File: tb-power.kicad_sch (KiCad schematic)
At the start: 56 parts, among them Q1 BC817-25W, U4 JHL6340SLLSQ

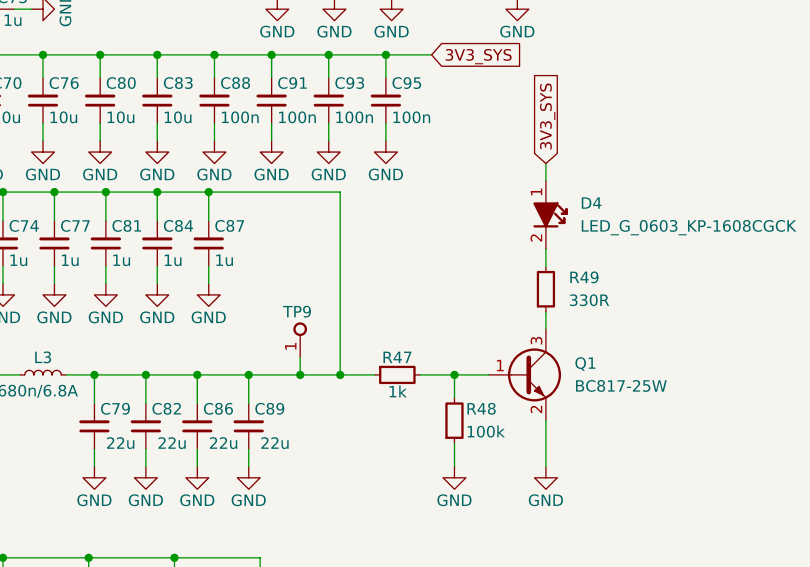
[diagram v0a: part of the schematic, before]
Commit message: Added switches for toggling PCIe power
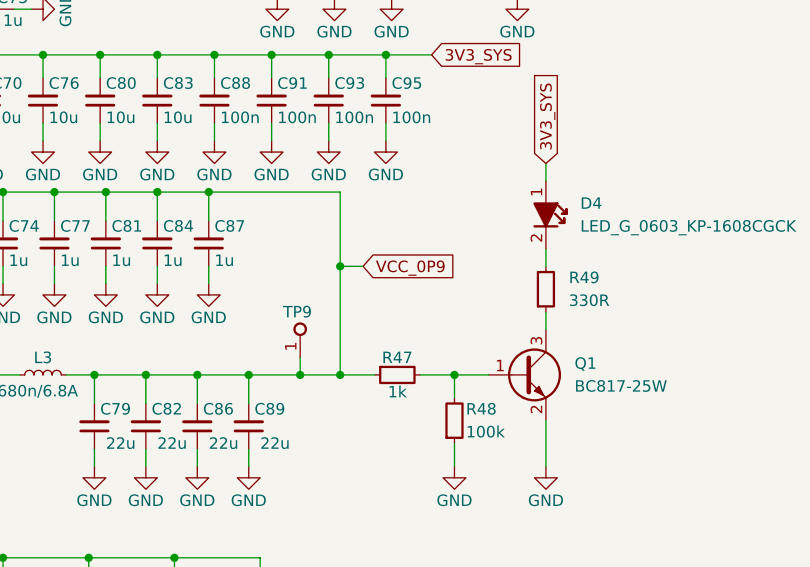
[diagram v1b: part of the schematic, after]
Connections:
- net VCC_0P9: now reaches C74.2, C77.2, C79.2, C81.2, C82.2, C84.2, C86.2, C87.2, C89.2, L3.2, R47.1, TP9.1, U4.E12 (VCC0P9_SVR_ANA), U4.E13 (VCC0P9_SVR_ANA), U4.F11 (VCC0P9_SVR_ANA), U4.F12 (VCC0P9_SVR_ANA), U4.F13 (VCC0P9_SVR_ANA), U4.F15 (VCC0P9_SVR_ANA), U4.J9 (VCC0P9_SVR_SENSE), U4.L9 (VCC0P9_SVR), U4.M9 (VCC0P9_SVR)
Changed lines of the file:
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@@
   (junction (at 174.625 85.09) (diameter 0) (color 0 0 0 0)
   )
+  (junction (at 218.44 113.665) (diameter 0) (color 0 0 0 0)
+  )
   (junction (at 116.205 92.71) (diameter 0) (color 0 0 0 0)
   )
@@
     (stroke (width 0) (type default) (color 0 0 0 0))
   )
+  (wire (pts (xy 218.44 113.665) (xy 218.44 125.73))
+    (stroke (width 0) (type default) (color 0 0 0 0))
+  )
   (wire (pts (xy 187.96 71.12) (xy 174.625 71.12))
     (stroke (width 0) (type default) (color 0 0 0 0))
@@
     (stroke (width 0) (type default) (color 0 0 0 0))
   )
-  (wire (pts (xy 218.44 105.41) (xy 218.44 125.73))
+  (wire (pts (xy 218.44 105.41) (xy 218.44 113.665))
     (stroke (width 0) (type default) (color 0 0 0 0))
   )
@@
   )
   (wire (pts (xy 175.26 265.43) (xy 175.26 267.97))
+    (stroke (width 0) (type default) (color 0 0 0 0))
+  )
+  (wire (pts (xy 218.44 113.665) (xy 220.98 113.665))
     (stroke (width 0) (type default) (color 0 0 0 0))
   )
@@
     (effects (font (size 2.54 2.54) (thickness 0.508) bold) (justify left bottom))
   )
+  (global_label "VCC_0P9" (shape input) (at 220.98 113.665 0) (fields_autoplaced)
+    (effects (font (size 1.27 1.27)) (justify left))
+    (property "Intersheet References" "${INTERSHEET_REFS}" (id 0) (at 231.6783 113.5856 0)
+      (effects (font (size 1.27 1.27)) (justify left) hide)
+    )
+  )
   (global_label "3V3_SYS" (shape input) (at 187.96 71.12 0) (fields_autoplaced)

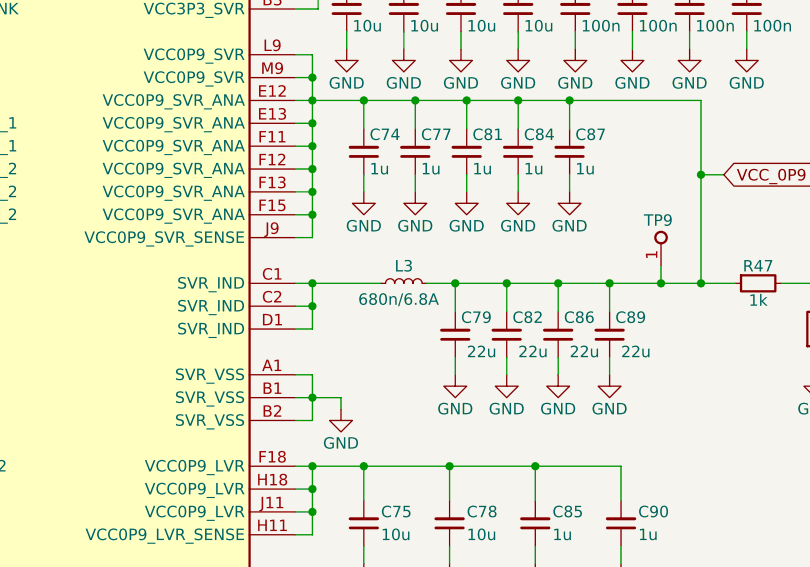
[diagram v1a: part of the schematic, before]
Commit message: [#49762] Fix missing 3D models
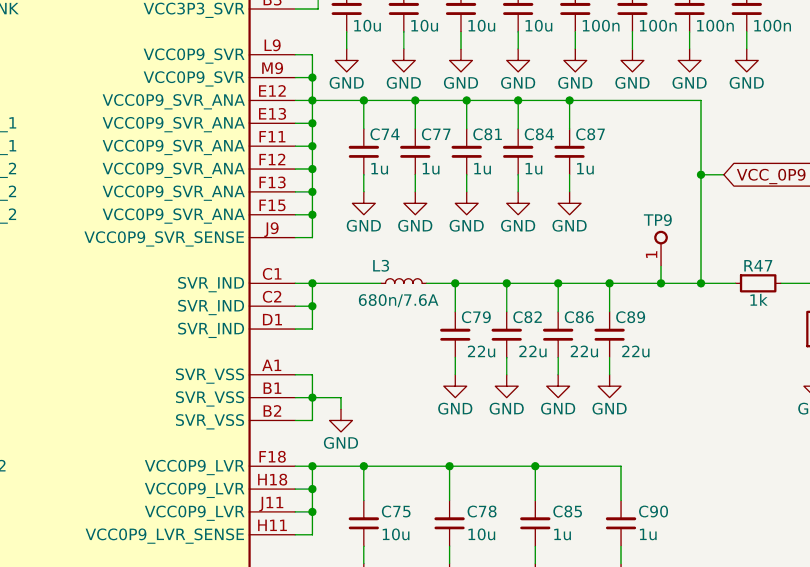
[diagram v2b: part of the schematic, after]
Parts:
- removed L3: L_680n_6.8A_IHLP1616BZ, antmicro-footprints:L_Vishay_IHLP1616BZ, symbol antmicroFixedInductors:L_680n_6.8A_IHLP1616BZ
- added L3: L_680n_7.6A_IHLP1616BZ, antmicro-footprints:L_Vishay-IHLP1616BZ, symbol antmicroFixedInductors:L_680n_7.6A_IHLP1616BZ
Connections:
- net VCC_0P9: now also L3.2
- net at U4.C1 (SVR_IND), U4.C2 (SVR_IND), U4.D1 (SVR_IND): now also L3.1
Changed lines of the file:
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@@
+    (pin "2")
+  )
+  (symbol (lib_id "antmicroFixedInductors:L_680n_7.6A_IHLP1616BZ") (at 182.88 125.73 0) (unit 1)
+    (in_bom yes) (on_board yes)
+    (property "Reference" "L3" (id 0) (at 182.88 123.825 0)
+      (effects (font (size 1.27 1.27) (thickness 0.15)))
+    )
+    (property "Value" "L_680n_7.6A_IHLP1616BZ" (id 1) (at 196.85 128.27 0)
+      (effects (font (size 1.27 1.27) (thickness 0.15)) (justify left bottom) hide)
+    )
+    (property "Footprint" "antmicro-footprints:L_Vishay-IHLP1616BZ" (id 2) (at 196.85 133.35 0)
+      (effects (font (size 1.27 1.27) (thickness 0.15)) (justify left bottom) hide)
+    )
+    (property "Datasheet" "https://www.mouser.com/datasheet/2/427/ihlp1616bz5a-1763007.pdf" (id 3) (at 196.85 135.89 0)
+      (effects (font (size 1.27 1.27) (thickness 0.15)) (justify left bottom) hide)
+    )
+    (property "Val" "680n/7.6A" (id 4) (at 184.785 127.635 0)
+      (effects (font (size 1.27 1.27) (thickness 0.15)))
+    )
+    (property "Manufacturer" "Vishay" (id 5) (at 196.85 138.43 0)
+      (effects (font (size 1.27 1.27) (thickness 0.15)) (justify left bottom) hide)
+    )
+    (property "MPN" "IHLP1616BZERR68M5A" (id 6) (at 196.85 140.97 0)
+      (effects (font (size 1.27 1.27) (thickness 0.15)) (justify left bottom) hide)
+    )
+    (property "ISat" "6.8 A" (id 7) (at 196.85 142.24 0)
+      (effects (font (size 1.27 1.27)) (justify left) hide)
+    )
+    (property "IMax" "7.6 A" (id 8) (at 196.85 146.05 0)
+      (effects (font (size 1.27 1.27) (thickness 0.15)) (justify left bottom) hide)
+    )
+    (property "Size" "4.06x4.06" (id 9) (at 196.85 148.59 0)
+      (effects (font (size 1.27 1.27) (thickness 0.15)) (justify left bottom) hide)
+    )
+    (property "Author" "Antmicro" (id 10) (at 196.85 151.13 0)
+      (effects (font (size 1.27 1.27) (thickness 0.15)) (justify left bottom) hide)
+    )
+    (property "License" "Apache-2.0" (id 11) (at 196.85 153.67 0)
+      (effects (font (size 1.27 1.27) (thickness 0.15)) (justify left bottom) hide)
+    )
+    (pin "1")
     (pin "2")
   )
@@
     (pin "1")
   )
-  (symbol (lib_id "antmicroFixedInductors:L_680n_6.8A_IHLP1616BZ") (at 182.88 125.73 0) (unit 1)
-    (in_bom yes) (on_board yes)
-    (property "Reference" "L3" (id 0) (at 185.42 123.825 0)
-      (effects (font (size 1.27 1.27) (thickness 0.15)))
-    )
-    (property "Value" "L_680n_6.8A_IHLP1616BZ" (id 1) (at 196.85 128.27 0)
-      (effects (font (size 1.27 1.27) (thickness 0.15)) (justify left bottom) hide)
-    )
-    (property "Footprint" "antmicro-footprints:L_Vishay_IHLP1616BZ" (id 2) (at 196.85 133.35 0)
-      (effects (font (size 1.27 1.27) (thickness 0.15)) (justify left bottom) hide)
-    )
-    (property "Datasheet" "https://www.mouser.pl/datasheet/2/427/ihlp1616bz5a-1763007.pdf" (id 3) (at 196.85 135.89 0)
-      (effects (font (size 1.27 1.27) (thickness 0.15)) (justify left bottom) hide)
-    )
-    (property "Val" "680n/6.8A" (id 4) (at 180.34 128.27 0)
-      (effects (font (size 1.27 1.27) (thickness 0.15)) (justify left bottom))
-    )
-    (property "Manufacturer" "Vishay" (id 5) (at 196.85 138.43 0)
-      (effects (font (size 1.27 1.27) (thickness 0.15)) (justify left bottom) hide)
-    )
-    (property "MPN" "IHLP1616BZERR68M5A" (id 6) (at 196.85 140.97 0)
-      (effects (font (size 1.27 1.27) (thickness 0.15)) (justify left bottom) hide)
-    )
-    (property "ISat" "6.8" (id 7) (at 196.85 142.24 0)
-      (effects (font (size 1.27 1.27)) (justify left) hide)
-    )
-    (property "IMax" "7.6" (id 8) (at 196.85 146.05 0)
-      (effects (font (size 1.27 1.27) (thickness 0.15)) (justify left bottom) hide)
-    )
-    (property "Size" "4.06x4.06" (id 9) (at 196.85 148.59 0)
-      (effects (font (size 1.27 1.27) (thickness 0.15)) (justify left bottom) hide)
-    )
-    (property "License" "Apache-2.0" (id 11) (at 196.85 153.67 0)
-      (effects (font (size 1.27 1.27) (thickness 0.15)) (justify left bottom) hide)
-    )
-    (property "Author" "Antmicro" (id 12) (at 196.85 151.13 0)
-      (effects (font (size 1.27 1.27) (thickness 0.15)) (justify left bottom) hide)
-    )
-    (pin "1")
-    (pin "2")
-  )
   (symbol (lib_id "antmicropower:GND") (at 211.455 83.82 0) (unit 1)
